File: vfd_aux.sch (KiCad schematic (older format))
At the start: 24 parts

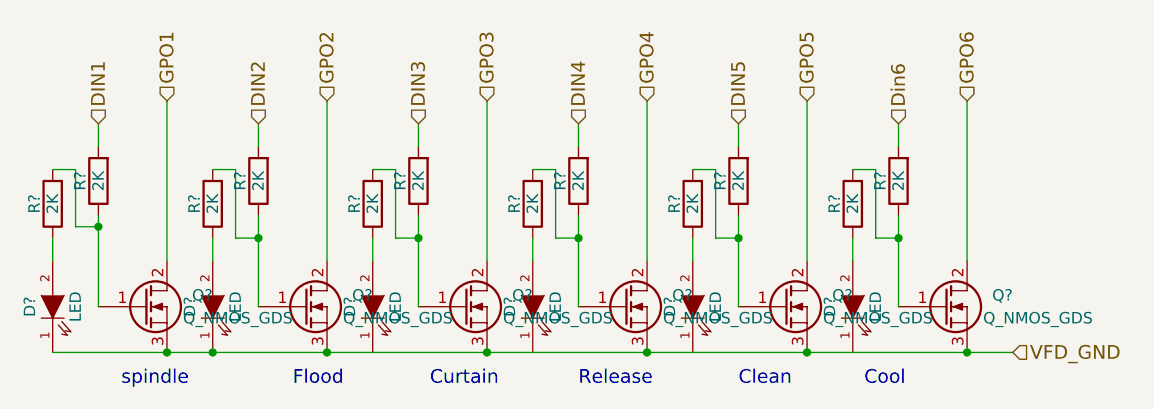
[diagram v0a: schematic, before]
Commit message: started pcb layout
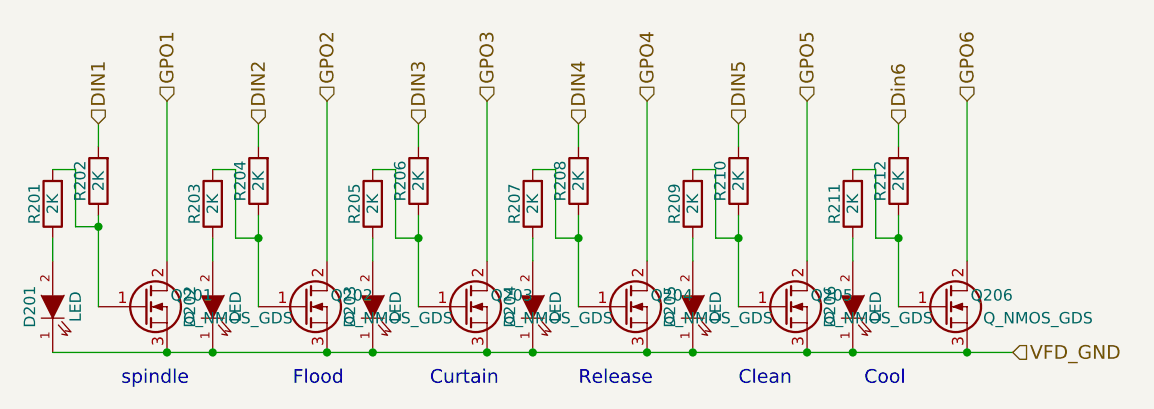
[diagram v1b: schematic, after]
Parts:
- gave numbers to parts that had none: 24
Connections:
- net VFD_GND: now also D203.1 (K), D204.1 (K), D205.1 (K), D206.1 (K)
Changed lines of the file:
@@
 $EndDescr
 $Comp
-L Q_NMOS_GDS Q?
+L Q_NMOS_GDS Q202
 U 1 1 5791C716
 P 4600 3900
-F 0 "Q?" H 4900 3950 50  0000 R CNN
+F 0 "Q202" H 4900 3950 50  0000 R CNN
 F 1 "Q_NMOS_GDS" H 5250 3850 50  0000 R CNN
 F 2 "TO_SOT_Packages_SMD:TO-252-2Lead" H 4800 4000 50  0001 C CNN
@@
 $EndComp
 $Comp
-L Q_NMOS_GDS Q?
+L Q_NMOS_GDS Q204
 U 1 1 5791C717
 P 6000 3900
-F 0 "Q?" H 6300 3950 50  0000 R CNN
+F 0 "Q204" H 6300 3950 50  0000 R CNN
 F 1 "Q_NMOS_GDS" H 6650 3850 50  0000 R CNN
 F 2 "TO_SOT_Packages_SMD:TO-252-2Lead" H 6200 4000 50  0001 C CNN
@@
 $EndComp
 $Comp
-L Q_NMOS_GDS Q?
+L Q_NMOS_GDS Q205
 U 1 1 5791C718
 P 6700 3900
-F 0 "Q?" H 7000 3950 50  0000 R CNN
+F 0 "Q205" H 7000 3950 50  0000 R CNN
 F 1 "Q_NMOS_GDS" H 7350 3850 50  0000 R CNN
 F 2 "TO_SOT_Packages_SMD:TO-252-2Lead" H 6900 4000 50  0001 C CNN
@@
 $EndComp
 $Comp
-L Q_NMOS_GDS Q?
+L Q_NMOS_GDS Q203
 U 1 1 5791C719
 P 5300 3900
-F 0 "Q?" H 5600 3950 50  0000 R CNN
+F 0 "Q203" H 5600 3950 50  0000 R CNN
 F 1 "Q_NMOS_GDS" H 5950 3850 50  0000 R CNN
 F 2 "TO_SOT_Packages_SMD:TO-252-2Lead" H 5500 4000 50  0001 C CNN
@@
 Curtain
 $Comp
-L Q_NMOS_GDS Q?
+L Q_NMOS_GDS Q206
 U 1 1 5791C71A
 P 7400 3900
-F 0 "Q?" H 7700 3950 50  0000 R CNN
+F 0 "Q206" H 7700 3950 50  0000 R CNN
 F 1 "Q_NMOS_GDS" H 8050 3850 50  0000 R CNN
 F 2 "TO_SOT_Packages_SMD:TO-252-2Lead" H 7600 4000 50  0001 C CNN
@@
 $EndComp
 $Comp
-L R R?
+L R R204
 U 1 1 5791C71B
 P 4400 3350
-F 0 "R?" V 4480 3350 50  0000 C CNN
+F 0 "R204" V 4480 3350 50  0000 C CNN
 F 1 "2K" V 4400 3350 50  0000 C CNN
 F 2 "Resistors_SMD:R_1206" V 4330 3350 50  0001 C CNN
@@
 $EndComp
 $Comp
-L R R?
+L R R206
 U 1 1 5791C71C
 P 5100 3350
-F 0 "R?" V 5180 3350 50  0000 C CNN
+F 0 "R206" V 5180 3350 50  0000 C CNN
 F 1 "2K" V 5100 3350 50  0000 C CNN
 F 2 "Resistors_SMD:R_1206" V 5030 3350 50  0001 C CNN
@@
 $EndComp
 $Comp
-L R R?
+L R R208
 U 1 1 5791C71D
 P 5800 3350
-F 0 "R?" V 5880 3350 50  0000 C CNN
+F 0 "R208" V 5880 3350 50  0000 C CNN
 F 1 "2K" V 5800 3350 50  0000 C CNN
 F 2 "Resistors_SMD:R_1206" V 5730 3350 50  0001 C CNN
@@
 $EndComp
 $Comp
-L R R?
+L R R210
 U 1 1 5791C71E
 P 6500 3350
-F 0 "R?" V 6580 3350 50  0000 C CNN
+F 0 "R210" V 6580 3350 50  0000 C CNN
 F 1 "2K" V 6500 3350 50  0000 C CNN
 F 2 "Resistors_SMD:R_1206" V 6430 3350 50  0001 C CNN
@@
 $EndComp
 $Comp
-L R R?
+L R R212
 U 1 1 5791C71F
 P 7200 3350
-F 0 "R?" V 7280 3350 50  0000 C CNN
+F 0 "R212" V 7280 3350 50  0000 C CNN
 F 1 "2K" V 7200 3350 50  0000 C CNN
 F 2 "Resistors_SMD:R_1206" V 7130 3350 50  0001 C CNN
@@
 spindle
 Wire Wire Line
-	3500 4100 4000 4100
-Wire Wire Line
-	4000 4100 4200 4100
-Wire Wire Line
-	4200 4100 4700 4100
-Wire Wire Line
-	4700 4100 5400 4100
-Wire Wire Line
-	5400 4100 6100 4100
-Wire Wire Line
-	6100 4100 6800 4100
-Wire Wire Line
-	6800 4100 7500 4100
-Wire Wire Line
-	7500 4100 7700 4100
+	3500 4100 7700 4100
 Connection ~ 6800 4100
 Connection ~ 6100 4100
 Connection ~ 5400 4100
 $Comp
-L Q_NMOS_GDS Q?
+L Q_NMOS_GDS Q201
 U 1 1 5791C720
 P 3900 3900
-F 0 "Q?" H 4200 3950 50  0000 R CNN
+F 0 "Q201" H 4200 3950 50  0000 R CNN
 F 1 "Q_NMOS_GDS" H 4550 3850 50  0000 R CNN
 F 2 "TO_SOT_Packages_SMD:TO-252-2Lead" H 4100 4000 50  0001 C CNN
@@
 $EndComp
 $Comp
-L R R?
+L R R202
 U 1 1 5791C721
 P 3700 3350
-F 0 "R?" V 3780 3350 50  0000 C CNN
+F 0 "R202" V 3780 3350 50  0000 C CNN
 F 1 "2K" V 3700 3350 50  0000 C CNN
 F 2 "Resistors_SMD:R_1206" V 3630 3350 50  0001 C CNN
@@
 	3700 3200 3700 3100
 Wire Wire Line
-	3700 3500 3700 3550
-Wire Wire Line
-	3700 3550 3700 3900
-Wire Wire Line
-	4400 3500 4400 3600
-Wire Wire Line
-	4400 3600 4400 3900
+	3700 3500 3700 3900
+Wire Wire Line
+	4400 3500 4400 3900
 Wire Wire Line
 	4400 3200 4400 3100
@@
 	5100 3100 5100 3200
 Wire Wire Line
-	5100 3500 5100 3600
-Wire Wire Line
-	5100 3600 5100 3900
-Wire Wire Line
-	5800 3500 5800 3600
-Wire Wire Line
-	5800 3600 5800 3900
+	5100 3500 5100 3900
+Wire Wire Line
+	5800 3500 5800 3900
 Wire Wire Line
 	5800 3200 5800 3100
@@
 	6500 3200 6500 3100
 Wire Wire Line
-	6500 3500 6500 3600
-Wire Wire Line
-	6500 3600 6500 3900
-Wire Wire Line
-	7200 3500 7200 3600
-Wire Wire Line
-	7200 3600 7200 3900
+	6500 3500 6500 3900
+Wire Wire Line
+	7200 3500 7200 3900
 Wire Wire Line
 	7200 3200 7200 3100
 $Comp
-L LED D?
+L LED D202
 U 1 1 5791C722
 P 4200 3900
-F 0 "D?" H 4200 4000 50  0000 C CNN
+F 0 "D202" H 4200 4000 50  0000 C CNN
 F 1 "LED" H 4200 3800 50  0000 C CNN
 F 2 "LEDs:LED_1206" H 4200 3900 50  0001 C CNN
@@
 Connection ~ 4200 4100
 $Comp
-L R R?
+L R R203
 U 1 1 5791C723
 P 4200 3450
-F 0 "R?" V 4280 3450 50  0000 C CNN
+F 0 "R203" V 4280 3450 50  0000 C CNN
 F 1 "2K" V 4200 3450 50  0000 C CNN
 F 2 "Resistors_SMD:R_1206" V 4130 3450 50  0001 C CNN
@@
 $EndComp
 $Comp
-L LED D?
+L LED D203
 U 1 1 5791C724
 P 4900 3900
-F 0 "D?" H 4900 4000 50  0000 C CNN
+F 0 "D203" H 4900 4000 50  0000 C CNN
 F 1 "LED" H 4900 3800 50  0000 C CNN
 F 2 "LEDs:LED_1206" H 4900 3900 50  0001 C CNN
@@
 $EndComp
 $Comp
-L R R?
+L R R205
 U 1 1 5791C725
 P 4900 3450
-F 0 "R?" V 4980 3450 50  0000 C CNN
+F 0 "R205" V 4980 3450 50  0000 C CNN
 F 1 "2K" V 4900 3450 50  0000 C CNN
 F 2 "Resistors_SMD:R_1206" V 4830 3450 50  0001 C CNN
@@
 $EndComp
 $Comp
-L LED D?
+L LED D204
 U 1 1 5791C726
 P 5600 3900
-F 0 "D?" H 5600 4000 50  0000 C CNN
+F 0 "D204" H 5600 4000 50  0000 C CNN
 F 1 "LED" H 5600 3800 50  0000 C CNN
 F 2 "LEDs:LED_1206" H 5600 3900 50  0001 C CNN
@@
 $EndComp
 $Comp
-L R R?
+L R R207
 U 1 1 5791C727
 P 5600 3450
-F 0 "R?" V 5680 3450 50  0000 C CNN
+F 0 "R207" V 5680 3450 50  0000 C CNN
 F 1 "2K" V 5600 3450 50  0000 C CNN
 F 2 "Resistors_SMD:R_1206" V 5530 3450 50  0001 C CNN
@@
 $EndComp
 $Comp
-L LED D?
+L LED D201
 U 1 1 5791C728
 P 3500 3900
-F 0 "D?" H 3500 4000 50  0000 C CNN
+F 0 "D201" H 3500 4000 50  0000 C CNN
 F 1 "LED" H 3500 3800 50  0000 C CNN
 F 2 "LEDs:LED_1206" H 3500 3900 50  0001 C CNN
@@
 $EndComp
 $Comp
-L R R?
+L R R201
 U 1 1 5791C729
 P 3500 3450
-F 0 "R?" V 3580 3450 50  0000 C CNN
+F 0 "R201" V 3580 3450 50  0000 C CNN
 F 1 "2K" V 3500 3450 50  0000 C CNN
 F 2 "Resistors_SMD:R_1206" V 3430 3450 50  0001 C CNN
@@
 $EndComp
 $Comp
-L LED D?
+L LED D205
 U 1 1 5791C72A
 P 6300 3900
-F 0 "D?" H 6300 4000 50  0000 C CNN
+F 0 "D205" H 6300 4000 50  0000 C CNN
 F 1 "LED" H 6300 3800 50  0000 C CNN
 F 2 "LEDs:LED_1206" H 6300 3900 50  0001 C CNN
@@
 $EndComp
 $Comp
-L R R?
+L R R209
 U 1 1 5791C72B
 P 6300 3450
-F 0 "R?" V 6380 3450 50  0000 C CNN
+F 0 "R209" V 6380 3450 50  0000 C CNN
 F 1 "2K" V 6300 3450 50  0000 C CNN
 F 2 "Resistors_SMD:R_1206" V 6230 3450 50  0001 C CNN
@@
 $EndComp
 $Comp
-L LED D?
+L LED D206
 U 1 1 5791C72C
 P 7000 3900
-F 0 "D?" H 7000 4000 50  0000 C CNN
+F 0 "D206" H 7000 4000 50  0000 C CNN
 F 1 "LED" H 7000 3800 50  0000 C CNN
 F 2 "LEDs:LED_1206" H 7000 3900 50  0001 C CNN
@@
 $EndComp
 $Comp
-L R R?
+L R R211
 U 1 1 5791C72D
 P 7000 3450
-F 0 "R?" V 7080 3450 50  0000 C CNN
+F 0 "R211" V 7080 3450 50  0000 C CNN
 F 1 "2K" V 7000 3450 50  0000 C CNN
 F 2 "Resistors_SMD:R_1206" V 6930 3450 50  0001 C CNN
@@
 Text HLabel 7700 4100 2    60   Input ~ 0
 VFD_GND
+Connection ~ 4900 4100
+Connection ~ 5600 4100
+Connection ~ 6300 4100
+Connection ~ 7000 4100
 $EndSCHEMATC
